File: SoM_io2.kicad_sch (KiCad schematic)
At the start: 1 part, among them J2 Hermaphroditic_Molex_203456-0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

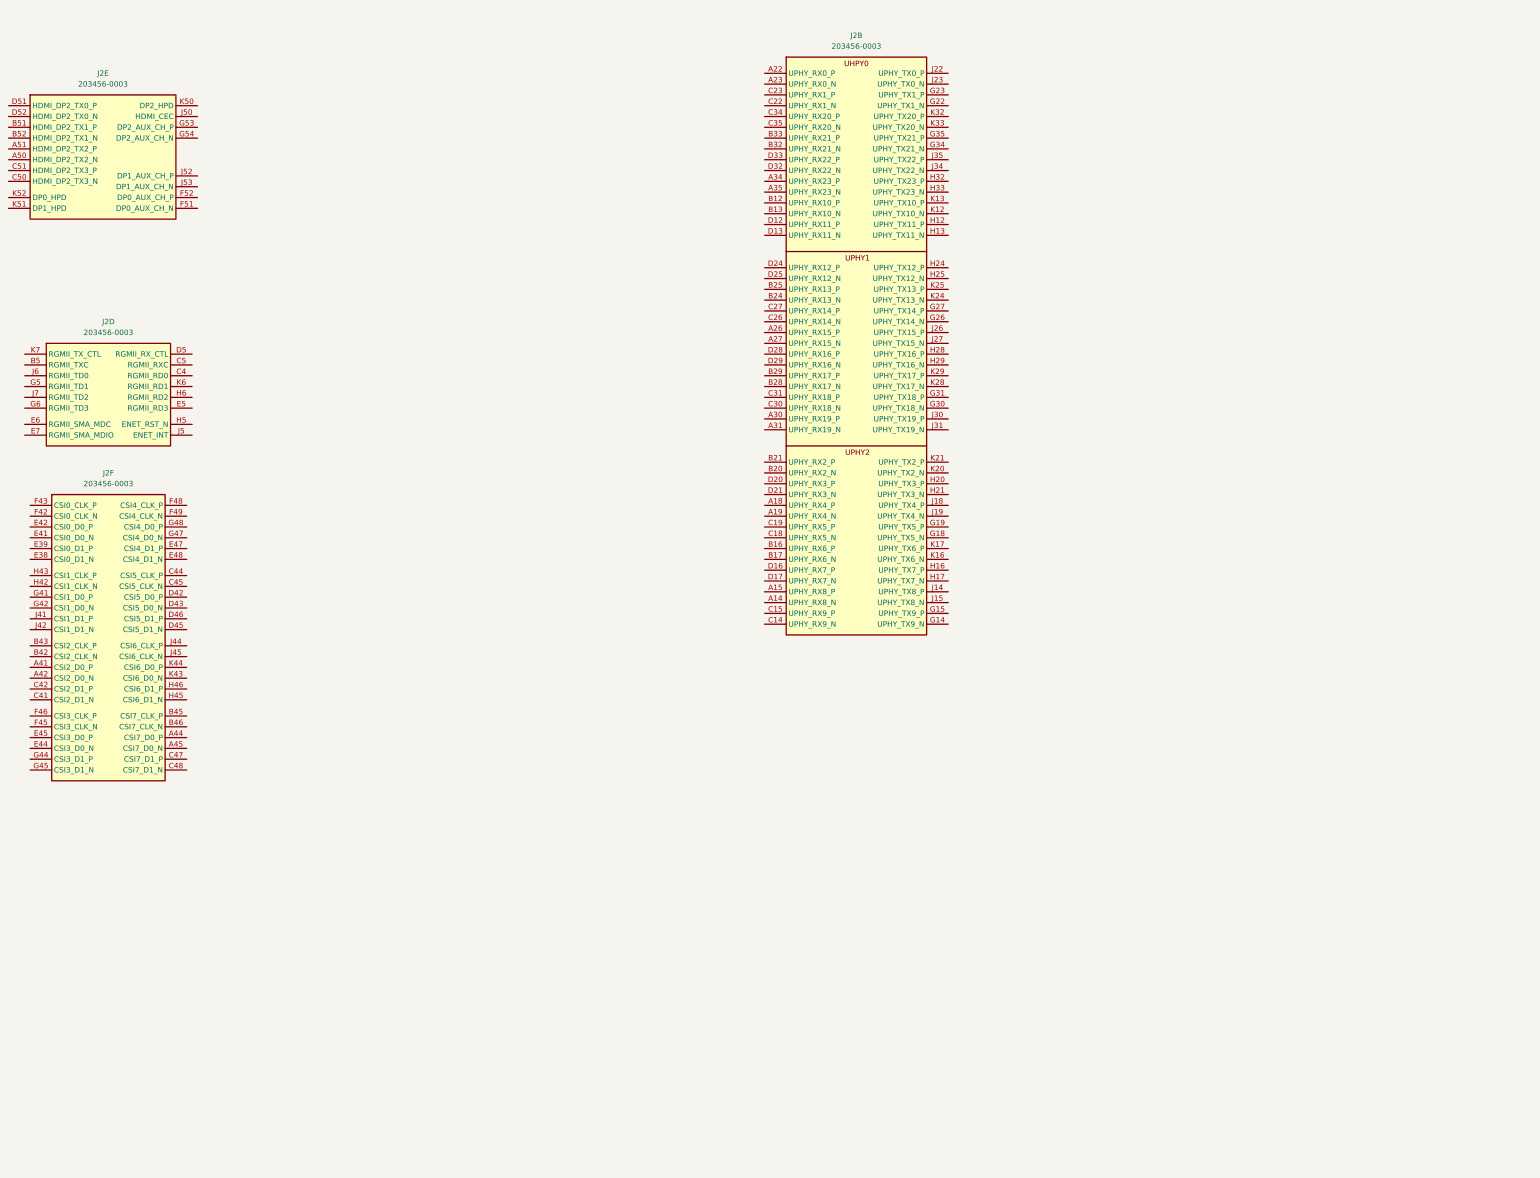
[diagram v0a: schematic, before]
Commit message: [#81778] Add 0R resistors
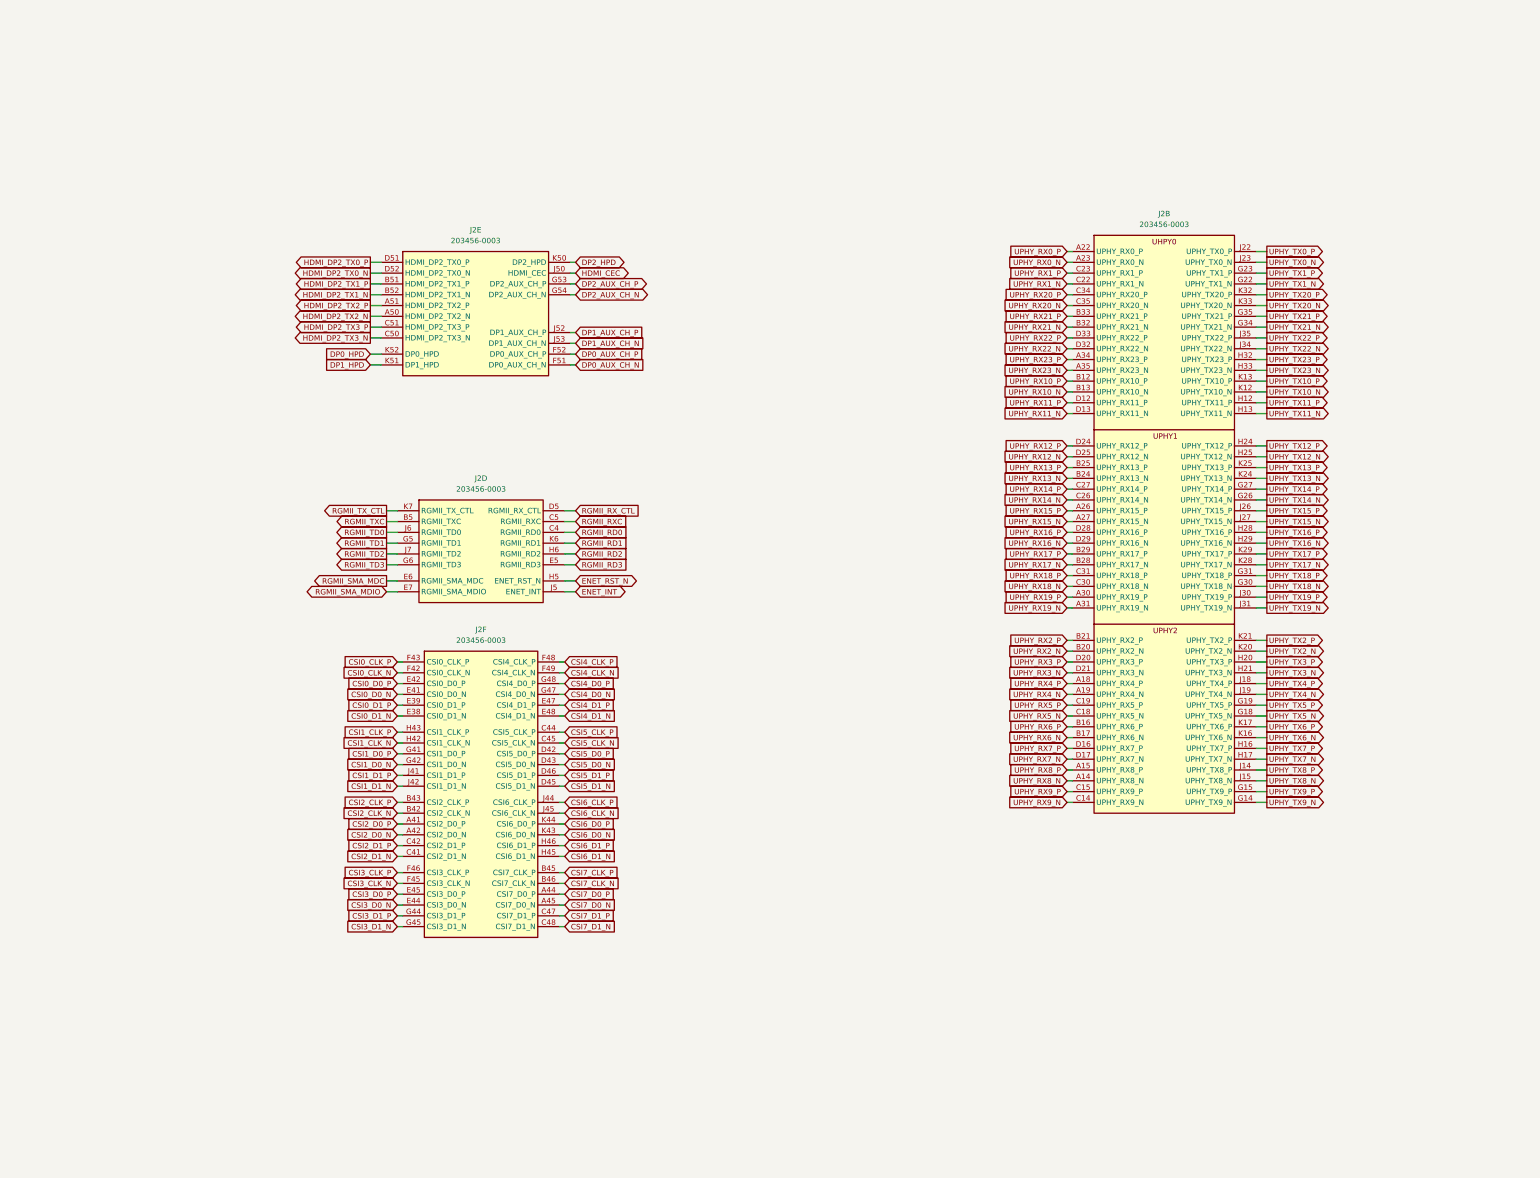
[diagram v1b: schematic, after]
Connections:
- net UPHY_RX8_N: now reaches J2.A14 (UPHY_RX8_N)
- net UPHY_RX8_P: now reaches J2.A15 (UPHY_RX8_P)
- net UPHY_RX4_P: now reaches J2.A18 (UPHY_RX4_P)
- net UPHY_RX4_N: now reaches J2.A19 (UPHY_RX4_N)
- net UPHY_RX0_P: now reaches J2.A22 (UPHY_RX0_P)
- net UPHY_RX0_N: now reaches J2.A23 (UPHY_RX0_N)
- net UPHY_RX15_P: now reaches J2.A26 (UPHY_RX15_P)
- net UPHY_RX15_N: now reaches J2.A27 (UPHY_RX15_N)
- net UPHY_RX19_P: now reaches J2.A30 (UPHY_RX19_P)
- net UPHY_RX19_N: now reaches J2.A31 (UPHY_RX19_N)
- net UPHY_RX23_P: now reaches J2.A34 (UPHY_RX23_P)
- net UPHY_RX23_N: now reaches J2.A35 (UPHY_RX23_N)
- net UPHY_RX10_P: now reaches J2.B12 (UPHY_RX10_P)
- net UPHY_RX10_N: now reaches J2.B13 (UPHY_RX10_N)
- net UPHY_RX6_P: now reaches J2.B16 (UPHY_RX6_P)
- net UPHY_RX6_N: now reaches J2.B17 (UPHY_RX6_N)
- net UPHY_RX2_N: now reaches J2.B20 (UPHY_RX2_N)
- net UPHY_RX2_P: now reaches J2.B21 (UPHY_RX2_P)
- net UPHY_RX13_N: now reaches J2.B24 (UPHY_RX13_N)
- net UPHY_RX13_P: now reaches J2.B25 (UPHY_RX13_P)
- net UPHY_RX17_N: now reaches J2.B28 (UPHY_RX17_N)
- net UPHY_RX17_P: now reaches J2.B29 (UPHY_RX17_P)
- net UPHY_RX21_N: now reaches J2.B32 (UPHY_RX21_N)
- net UPHY_RX21_P: now reaches J2.B33 (UPHY_RX21_P)
- net UPHY_RX9_N: now reaches J2.C14 (UPHY_RX9_N)
- net UPHY_RX9_P: now reaches J2.C15 (UPHY_RX9_P)
- net UPHY_RX5_N: now reaches J2.C18 (UPHY_RX5_N)
- net UPHY_RX5_P: now reaches J2.C19 (UPHY_RX5_P)
- net UPHY_RX1_N: now reaches J2.C22 (UPHY_RX1_N)
- net UPHY_RX1_P: now reaches J2.C23 (UPHY_RX1_P)
- net UPHY_RX14_N: now reaches J2.C26 (UPHY_RX14_N)
- net UPHY_RX14_P: now reaches J2.C27 (UPHY_RX14_P)
- net UPHY_RX18_N: now reaches J2.C30 (UPHY_RX18_N)
- net UPHY_RX18_P: now reaches J2.C31 (UPHY_RX18_P)
- net UPHY_RX20_P: now reaches J2.C34 (UPHY_RX20_P)
- net UPHY_RX20_N: now reaches J2.C35 (UPHY_RX20_N)
- net UPHY_RX11_P: now reaches J2.D12 (UPHY_RX11_P)
- net UPHY_RX11_N: now reaches J2.D13 (UPHY_RX11_N)
- net UPHY_RX7_P: now reaches J2.D16 (UPHY_RX7_P)
- net UPHY_RX7_N: now reaches J2.D17 (UPHY_RX7_N)
- net UPHY_RX3_P: now reaches J2.D20 (UPHY_RX3_P)
- net UPHY_RX3_N: now reaches J2.D21 (UPHY_RX3_N)
- net UPHY_RX12_P: now reaches J2.D24 (UPHY_RX12_P)
- net UPHY_RX12_N: now reaches J2.D25 (UPHY_RX12_N)
- net UPHY_RX16_P: now reaches J2.D28 (UPHY_RX16_P)
- net UPHY_RX16_N: now reaches J2.D29 (UPHY_RX16_N)
- net UPHY_RX22_N: now reaches J2.D32 (UPHY_RX22_N)
- net UPHY_RX22_P: now reaches J2.D33 (UPHY_RX22_P)
- net UPHY_TX9_N: now reaches J2.G14 (UPHY_TX9_N)
- net UPHY_TX9_P: now reaches J2.G15 (UPHY_TX9_P)
- net UPHY_TX5_N: now reaches J2.G18 (UPHY_TX5_N)
- net UPHY_TX5_P: now reaches J2.G19 (UPHY_TX5_P)
- net UPHY_TX1_N: now reaches J2.G22 (UPHY_TX1_N)
- net UPHY_TX1_P: now reaches J2.G23 (UPHY_TX1_P)
- net UPHY_TX14_N: now reaches J2.G26 (UPHY_TX14_N)
- net UPHY_TX14_P: now reaches J2.G27 (UPHY_TX14_P)
- net UPHY_TX18_N: now reaches J2.G30 (UPHY_TX18_N)
- net UPHY_TX18_P: now reaches J2.G31 (UPHY_TX18_P)
- net UPHY_TX21_N: now reaches J2.G34 (UPHY_TX21_N)
- net UPHY_TX21_P: now reaches J2.G35 (UPHY_TX21_P)
- net UPHY_TX11_P: now reaches J2.H12 (UPHY_TX11_P)
- net UPHY_TX11_N: now reaches J2.H13 (UPHY_TX11_N)
- net UPHY_TX7_P: now reaches J2.H16 (UPHY_TX7_P)
- net UPHY_TX7_N: now reaches J2.H17 (UPHY_TX7_N)
- net UPHY_TX3_P: now reaches J2.H20 (UPHY_TX3_P)
- net UPHY_TX3_N: now reaches J2.H21 (UPHY_TX3_N)
- net UPHY_TX12_P: now reaches J2.H24 (UPHY_TX12_P)
- net UPHY_TX12_N: now reaches J2.H25 (UPHY_TX12_N)
- net UPHY_TX16_P: now reaches J2.H28 (UPHY_TX16_P)
- net UPHY_TX16_N: now reaches J2.H29 (UPHY_TX16_N)
- net UPHY_TX23_P: now reaches J2.H32 (UPHY_TX23_P)
- net UPHY_TX23_N: now reaches J2.H33 (UPHY_TX23_N)
- net UPHY_TX8_P: now reaches J2.J14 (UPHY_TX8_P)
- net UPHY_TX8_N: now reaches J2.J15 (UPHY_TX8_N)
- net UPHY_TX4_P: now reaches J2.J18 (UPHY_TX4_P)
- net UPHY_TX4_N: now reaches J2.J19 (UPHY_TX4_N)
- net UPHY_TX0_P: now reaches J2.J22 (UPHY_TX0_P)
- net UPHY_TX0_N: now reaches J2.J23 (UPHY_TX0_N)
- net UPHY_TX15_P: now reaches J2.J26 (UPHY_TX15_P)
- net UPHY_TX15_N: now reaches J2.J27 (UPHY_TX15_N)
- net UPHY_TX19_P: now reaches J2.J30 (UPHY_TX19_P)
- net UPHY_TX19_N: now reaches J2.J31 (UPHY_TX19_N)
- net UPHY_TX22_N: now reaches J2.J34 (UPHY_TX22_N)
- net UPHY_TX22_P: now reaches J2.J35 (UPHY_TX22_P)
- net UPHY_TX10_N: now reaches J2.K12 (UPHY_TX10_N)
- net UPHY_TX10_P: now reaches J2.K13 (UPHY_TX10_P)
- net UPHY_TX6_N: now reaches J2.K16 (UPHY_TX6_N)
- net UPHY_TX6_P: now reaches J2.K17 (UPHY_TX6_P)
- net UPHY_TX2_N: now reaches J2.K20 (UPHY_TX2_N)
- net UPHY_TX2_P: now reaches J2.K21 (UPHY_TX2_P)
- net UPHY_TX13_N: now reaches J2.K24 (UPHY_TX13_N)
- net UPHY_TX13_P: now reaches J2.K25 (UPHY_TX13_P)
- net UPHY_TX17_N: now reaches J2.K28 (UPHY_TX17_N)
- net UPHY_TX17_P: now reaches J2.K29 (UPHY_TX17_P)
- net UPHY_TX20_P: now reaches J2.K32 (UPHY_TX20_P)
- net UPHY_TX20_N: now reaches J2.K33 (UPHY_TX20_N)
- net RGMII_TXC: now reaches J2.B5 (RGMII_TXC)
- net RGMII_RD0: now reaches J2.C4 (RGMII_RD0)
- net RGMII_RXC: now reaches J2.C5 (RGMII_RXC)
- net RGMII_RX_CTL: now reaches J2.D5 (RGMII_RX_CTL)
- net RGMII_RD3: now reaches J2.E5 (RGMII_RD3)
- net RGMII_SMA_MDC: now reaches J2.E6 (RGMII_SMA_MDC)
- net RGMII_SMA_MDIO: now reaches J2.E7 (RGMII_SMA_MDIO)
- net RGMII_TD1: now reaches J2.G5 (RGMII_TD1)
- net RGMII_TD3: now reaches J2.G6 (RGMII_TD3)
- net ENET_RST_N: now reaches J2.H5 (ENET_RST_N)
- net RGMII_RD2: now reaches J2.H6 (RGMII_RD2)
- net ENET_INT: now reaches J2.J5 (ENET_INT)
- net RGMII_TD0: now reaches J2.J6 (RGMII_TD0)
- net RGMII_TD2: now reaches J2.J7 (RGMII_TD2)
- net RGMII_RD1: now reaches J2.K6 (RGMII_RD1)
- net RGMII_TX_CTL: now reaches J2.K7 (RGMII_TX_CTL)
- net CSI2_D0_P: now reaches J2.A41 (CSI2_D0_P)
- net CSI2_D0_N: now reaches J2.A42 (CSI2_D0_N)
- net CSI7_D0_P: now reaches J2.A44 (CSI7_D0_P)
- net CSI7_D0_N: now reaches J2.A45 (CSI7_D0_N)
- net CSI2_CLK_N: now reaches J2.B42 (CSI2_CLK_N)
- net CSI2_CLK_P: now reaches J2.B43 (CSI2_CLK_P)
- net CSI7_CLK_P: now reaches J2.B45 (CSI7_CLK_P)
- net CSI7_CLK_N: now reaches J2.B46 (CSI7_CLK_N)
- net CSI2_D1_N: now reaches J2.C41 (CSI2_D1_N)
- net CSI2_D1_P: now reaches J2.C42 (CSI2_D1_P)
- net CSI5_CLK_P: now reaches J2.C44 (CSI5_CLK_P)
- net CSI5_CLK_N: now reaches J2.C45 (CSI5_CLK_N)
- net CSI7_D1_P: now reaches J2.C47 (CSI7_D1_P)
- net CSI7_D1_N: now reaches J2.C48 (CSI7_D1_N)
- net CSI5_D0_P: now reaches J2.D42 (CSI5_D0_P)
- net CSI5_D0_N: now reaches J2.D43 (CSI5_D0_N)
- net CSI5_D1_N: now reaches J2.D45 (CSI5_D1_N)
- net CSI5_D1_P: now reaches J2.D46 (CSI5_D1_P)
- net CSI0_D1_N: now reaches J2.E38 (CSI0_D1_N)
- net CSI0_D1_P: now reaches J2.E39 (CSI0_D1_P)
- net CSI0_D0_N: now reaches J2.E41 (CSI0_D0_N)
- net CSI0_D0_P: now reaches J2.E42 (CSI0_D0_P)
- net CSI3_D0_N: now reaches J2.E44 (CSI3_D0_N)
- net CSI3_D0_P: now reaches J2.E45 (CSI3_D0_P)
- net CSI4_D1_P: now reaches J2.E47 (CSI4_D1_P)
- net CSI4_D1_N: now reaches J2.E48 (CSI4_D1_N)
- net CSI0_CLK_N: now reaches J2.F42 (CSI0_CLK_N)
- net CSI0_CLK_P: now reaches J2.F43 (CSI0_CLK_P)
- net CSI3_CLK_N: now reaches J2.F45 (CSI3_CLK_N)
- net CSI3_CLK_P: now reaches J2.F46 (CSI3_CLK_P)
- net CSI4_CLK_P: now reaches J2.F48 (CSI4_CLK_P)
- net CSI4_CLK_N: now reaches J2.F49 (CSI4_CLK_N)
- net CSI1_D0_P: now reaches J2.G41 (CSI1_D0_P)
- net CSI1_D0_N: now reaches J2.G42 (CSI1_D0_N)
- net CSI3_D1_P: now reaches J2.G44 (CSI3_D1_P)
- net CSI3_D1_N: now reaches J2.G45 (CSI3_D1_N)
- net CSI4_D0_N: now reaches J2.G47 (CSI4_D0_N)
- net CSI4_D0_P: now reaches J2.G48 (CSI4_D0_P)
- net CSI1_CLK_N: now reaches J2.H42 (CSI1_CLK_N)
- net CSI1_CLK_P: now reaches J2.H43 (CSI1_CLK_P)
- net CSI6_D1_N: now reaches J2.H45 (CSI6_D1_N)
- net CSI6_D1_P: now reaches J2.H46 (CSI6_D1_P)
- net CSI1_D1_P: now reaches J2.J41 (CSI1_D1_P)
- net CSI1_D1_N: now reaches J2.J42 (CSI1_D1_N)
- net CSI6_CLK_P: now reaches J2.J44 (CSI6_CLK_P)
- net CSI6_CLK_N: now reaches J2.J45 (CSI6_CLK_N)
- net CSI6_D0_N: now reaches J2.K43 (CSI6_D0_N)
- net CSI6_D0_P: now reaches J2.K44 (CSI6_D0_P)
- net HDMI_DP2_TX2_N: now reaches J2.A50 (HDMI_DP2_TX2_N)
- net HDMI_DP2_TX2_P: now reaches J2.A51 (HDMI_DP2_TX2_P)
- net HDMI_DP2_TX1_P: now reaches J2.B51 (HDMI_DP2_TX1_P)
- net HDMI_DP2_TX1_N: now reaches J2.B52 (HDMI_DP2_TX1_N)
- net HDMI_DP2_TX3_N: now reaches J2.C50 (HDMI_DP2_TX3_N)
- net HDMI_DP2_TX3_P: now reaches J2.C51 (HDMI_DP2_TX3_P)
- net HDMI_DP2_TX0_P: now reaches J2.D51 (HDMI_DP2_TX0_P)
- net HDMI_DP2_TX0_N: now reaches J2.D52 (HDMI_DP2_TX0_N)
- net DP0_AUX_CH_N: now reaches J2.F51 (DP0_AUX_CH_N)
- net DP0_AUX_CH_P: now reaches J2.F52 (DP0_AUX_CH_P)
- net DP2_AUX_CH_P: now reaches J2.G53 (DP2_AUX_CH_P)
- net DP2_AUX_CH_N: now reaches J2.G54 (DP2_AUX_CH_N)
- net HDMI_CEC: now reaches J2.J50 (HDMI_CEC)
- net DP1_AUX_CH_P: now reaches J2.J52 (DP1_AUX_CH_P)
- net DP1_AUX_CH_N: now reaches J2.J53 (DP1_AUX_CH_N)
- net DP2_HPD: now reaches J2.K50 (DP2_HPD)
- net DP1_HPD: now reaches J2.K51 (DP1_HPD)
- net DP0_HPD: now reaches J2.K52 (DP0_HPD)
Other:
- moved on the sheet: J2B, J2D, J2E, J2F

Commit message: [#81970] Refactor root
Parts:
- renumbered J2 to J1
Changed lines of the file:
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@@
 		(on_board yes)
 		(dnp no)
-		(property "Reference" "J2"
+		(property "Reference" "J1"
 			(at 295.91 59.69 0)
 			(effects
@@
 		(instances
 			(project "jetson-orin-agx-baseboard"
-				(path "/f569b0be-0afd-48b7-93ee-28582a4c645c/4579c4a7-22a6-485d-a5cb-a4d2e4f367db/f334e2db-25af-407f-a645-338d24a757e4"
-					(reference "J2")
+				(path "/f569b0be-0afd-48b7-93ee-28582a4c645c/656db8bb-c788-4c93-9592-ce18fa1a48a2"
+					(reference "J1")
 					(unit 2)
 				)
@@
 		(dnp no)
 		(fields_autoplaced yes)
-		(property "Reference" "J2"
+		(property "Reference" "J1"
 			(at 135.255 121.92 0)
 			(effects
@@
 		(instances
 			(project "jetson-orin-agx-baseboard"
-				(path "/f569b0be-0afd-48b7-93ee-28582a4c645c/4579c4a7-22a6-485d-a5cb-a4d2e4f367db/f334e2db-25af-407f-a645-338d24a757e4"
-					(reference "J2")
+				(path "/f569b0be-0afd-48b7-93ee-28582a4c645c/656db8bb-c788-4c93-9592-ce18fa1a48a2"
+					(reference "J1")
 					(unit 4)
 				)
@@
 		(dnp no)
 		(fields_autoplaced yes)
-		(property "Reference" "J2"
+		(property "Reference" "J1"
 			(at 135.255 157.48 0)
 			(effects
@@
 		(instances
 			(project "jetson-orin-agx-baseboard"
-				(path "/f569b0be-0afd-48b7-93ee-28582a4c645c/4579c4a7-22a6-485d-a5cb-a4d2e4f367db/f334e2db-25af-407f-a645-338d24a757e4"
-					(reference "J2")
+				(path "/f569b0be-0afd-48b7-93ee-28582a4c645c/656db8bb-c788-4c93-9592-ce18fa1a48a2"
+					(reference "J1")
 					(unit 6)
 				)
@@
 		(dnp no)
 		(fields_autoplaced yes)
-		(property "Reference" "J2"
+		(property "Reference" "J1"
 			(at 133.985 63.5 0)
 			(effects
@@
 		(instances
 			(project "jetson-orin-agx-baseboard"
-				(path "/f569b0be-0afd-48b7-93ee-28582a4c645c/4579c4a7-22a6-485d-a5cb-a4d2e4f367db/f334e2db-25af-407f-a645-338d24a757e4"
-					(reference "J2")
+				(path "/f569b0be-0afd-48b7-93ee-28582a4c645c/656db8bb-c788-4c93-9592-ce18fa1a48a2"
+					(reference "J1")
 					(unit 5)
 				)

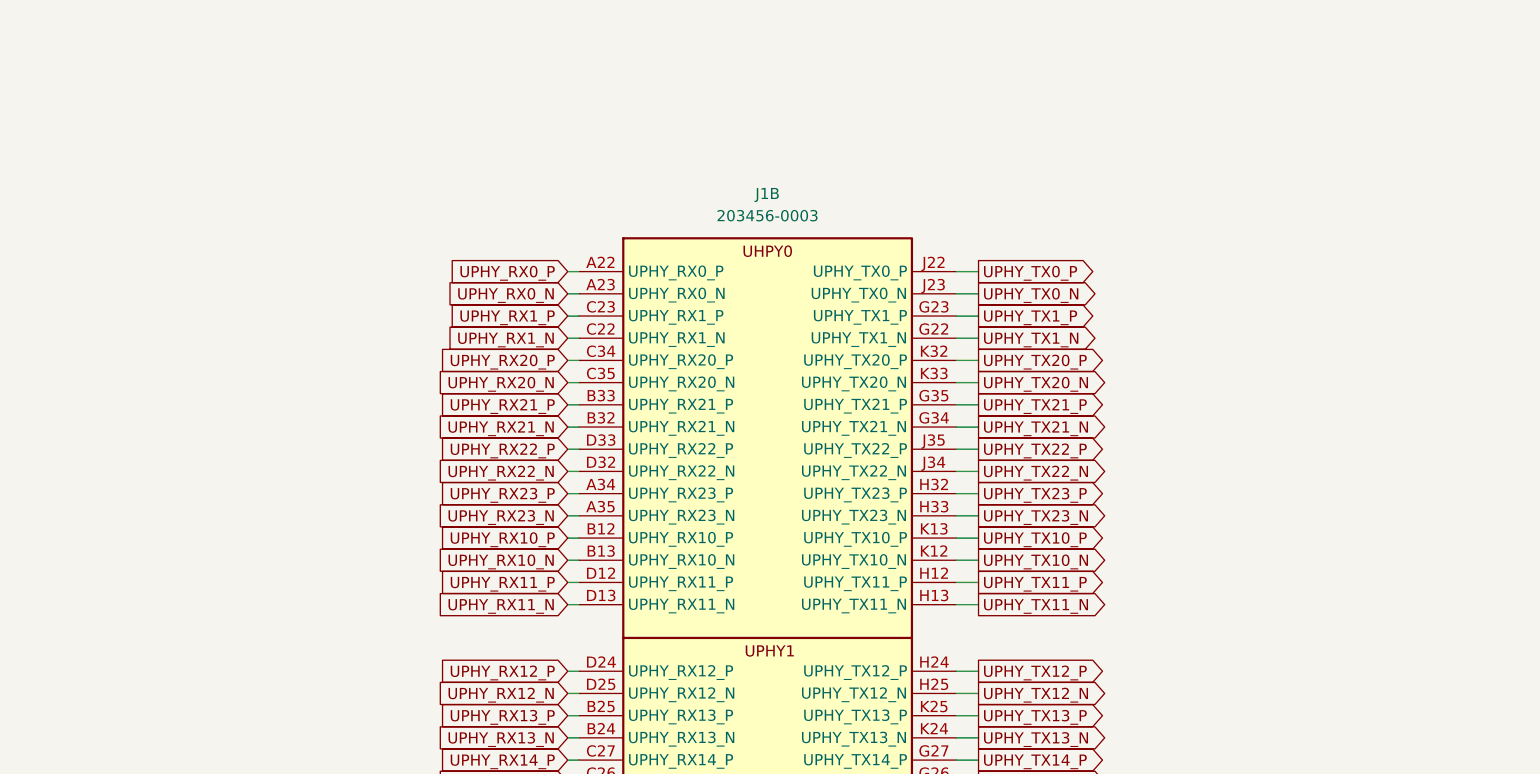
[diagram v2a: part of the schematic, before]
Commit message: [#82048] Add bus definitions and bus connections from M.2 key M to SoM
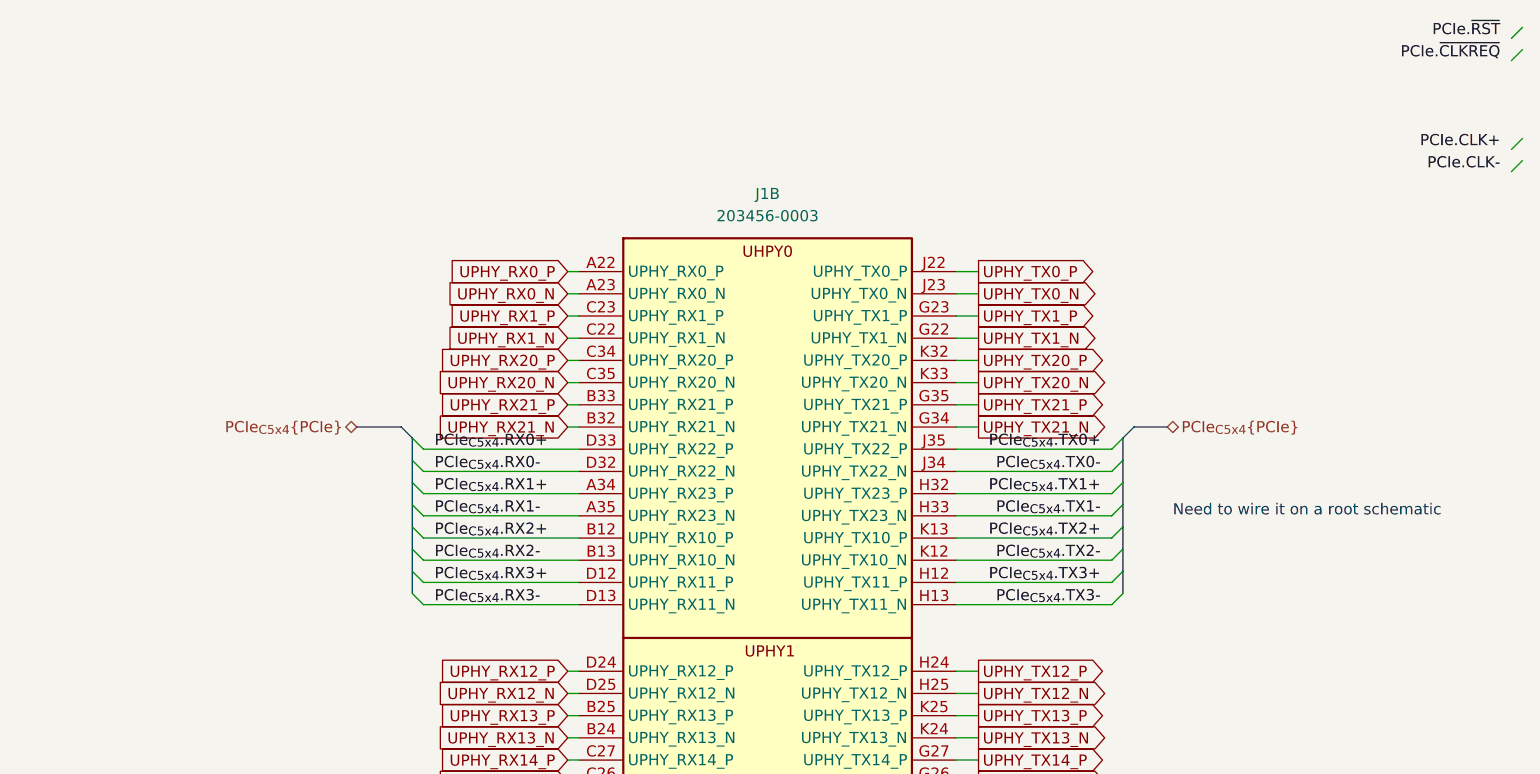
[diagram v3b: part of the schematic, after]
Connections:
- net UPHY_RX10_N renamed PCIe_{C5x4}.RX2-
- net UPHY_RX10_P renamed PCIe_{C5x4}.RX2+
- net UPHY_RX11_N renamed PCIe_{C5x4}.RX3-
- net UPHY_RX11_P renamed PCIe_{C5x4}.RX3+
- net UPHY_RX22_N renamed PCIe_{C5x4}.RX0-
- net UPHY_RX22_P renamed PCIe_{C5x4}.RX0+
- net UPHY_RX23_N renamed PCIe_{C5x4}.RX1-
- net UPHY_RX23_P renamed PCIe_{C5x4}.RX1+
- net UPHY_TX10_N renamed PCIe_{C5x4}.TX2-
- net UPHY_TX10_P renamed PCIe_{C5x4}.TX2+
- net UPHY_TX11_N renamed PCIe_{C5x4}.TX3-
- net UPHY_TX11_P renamed PCIe_{C5x4}.TX3+
- net UPHY_TX22_N renamed PCIe_{C5x4}.TX0-
- net UPHY_TX22_P renamed PCIe_{C5x4}.TX0+
- net UPHY_TX23_N renamed PCIe_{C5x4}.TX1-
- net UPHY_TX23_P renamed PCIe_{C5x4}.TX1+
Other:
- note added: "Need to wire it on a root schematic"
